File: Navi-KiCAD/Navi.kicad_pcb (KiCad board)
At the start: 4 copper layers, 50.8 x 40 mm, 207 parts, among them J1 0734120110, J2 0734120110, J3 0734120110, J4 473460001, J5 AXK5S80047YG, J6 AXK5S80047YG, Q1 IRLML5203PbF, Q2 IRLML5203PbF, U1 LP5521YQ/NOPB, U10 TPS54232DR, U11 MPU-9250, U12 LPS25HBTR, U13 NUF2042XV6T1G, U14 LTC4412ES6, U15 MIC94082YFT, U2 Logo, U3 Logo, U4 ATSAME70Q21A-AN, U5 CC1310F128RGZR, U6 CC1190RGVR, U7 CC2650F128RGZR, U8 CC2592RGVR, U9 MAX-M8W-0, Y1 9HT11-32.768KDZB-T, Y2 7V-16.000MAHJ-T, Y3 XRCGB24M000F2P00R0, Y4 XRCGB24M000F2P00R0

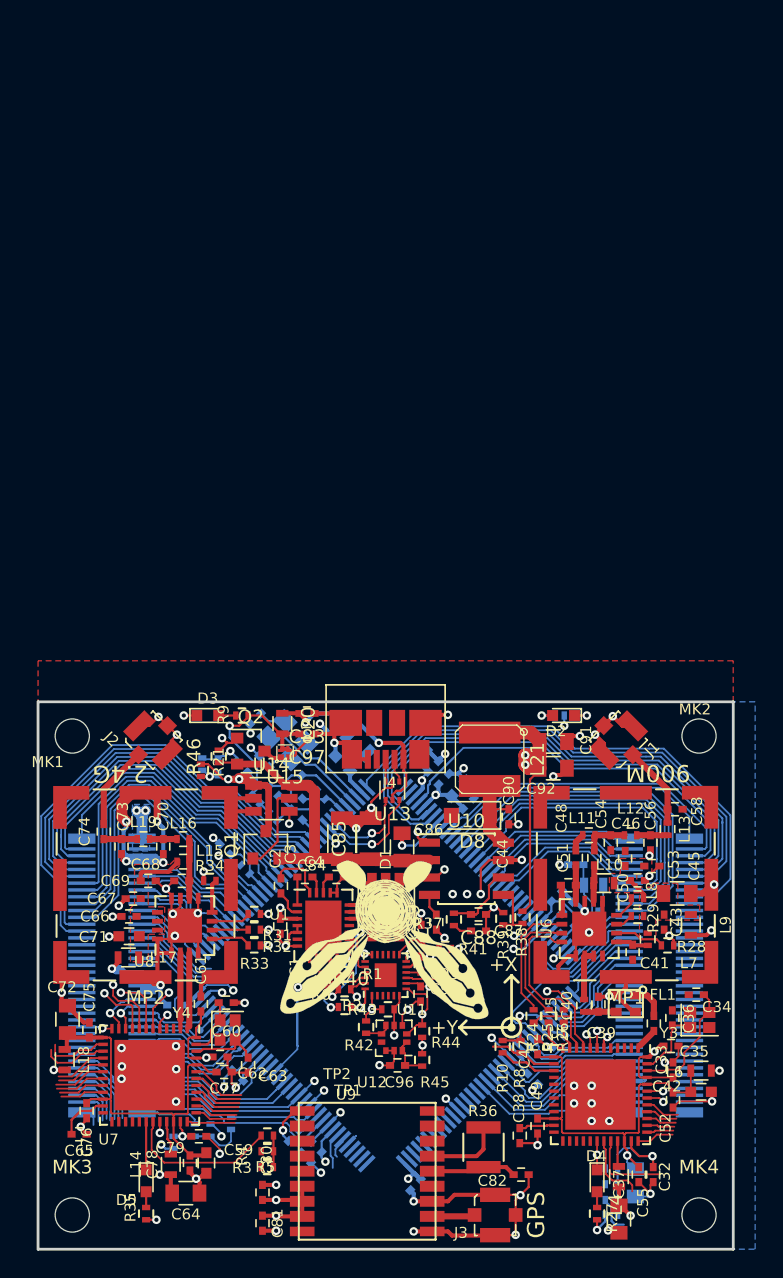
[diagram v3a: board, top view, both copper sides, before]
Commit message: Additional routing
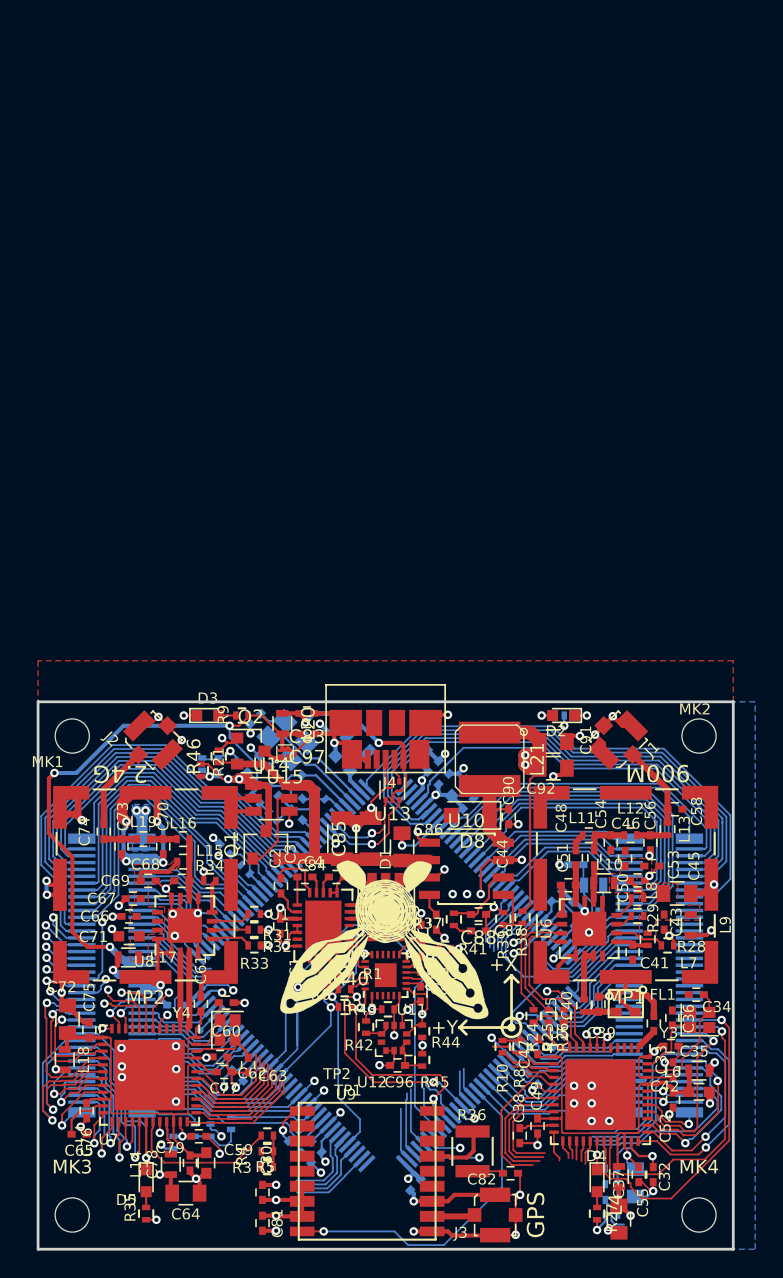
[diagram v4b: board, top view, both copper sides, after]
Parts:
- Q1, Q2: value IRLML5203PbF -> IRLML5203TRPBF
- U14: value LTC4412ES6 -> LTC4412ES6#TRPBF
- U15: value MIC94082YFT -> MIC94082YFT-TR
- moved R36 0.85 mm to (81.3, 117.8)
- moved C82 0.78 mm to (84.1, 119.5)
- moved C42 0.15 mm to (97.9, 113.5)
- moved L6 0.15 mm to (97.9, 112.0)
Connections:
- J5 pad 35: Net-(J5-Pad35) -> VUSB
- J5 pad 37: Net-(J5-Pad37) -> VUSB
- J5 pad 50: Net-(J5-Pad50) -> /Connectors/2.4-DIO-10
- J5 pad 52: Net-(J5-Pad52) -> /Connectors/2.4-DIO-9
- J5 pad 54: Net-(J5-Pad54) -> /Connectors/2.4-DIO-8
- J5 pad 58: Net-(J5-Pad58) -> /Connectors/2.4-DIO-20
- J5 pad 60: Net-(J5-Pad60) -> /Connectors/2.4-DIO-11
- J5 pad 62: Net-(J5-Pad62) -> /Connectors/2.4-DIO-19
- J5 pad 64: Net-(J5-Pad64) -> /Connectors/2.4-DIO-12
- J5 pad 66: Net-(J5-Pad66) -> /Connectors/2.4-DIO-18
- J5 pad 68: Net-(J5-Pad68) -> /Connectors/2.4-DIO-13
- J5 pad 70: Net-(J5-Pad70) -> /Connectors/2.4-DIO-17
- J5 pad 72: Net-(J5-Pad72) -> /Connectors/2.4-DIO-14
- J5 pad 74: Net-(J5-Pad74) -> /Connectors/2.4-DIO-16
- J5 pad 76: Net-(J5-Pad76) -> /2.4-TCKC
- J5 pad 78: Net-(J5-Pad78) -> /2.4-TMSC
- J5 pad 80: Net-(J5-Pad80) -> /Connectors/2.4-DIO-15
- J6 pad 28: Net-(J6-Pad28) -> /Connectors/PE5
- J6 pad 53: Net-(J6-Pad53) -> /Connectors/900-DIO-21
- J6 pad 55: Net-(J6-Pad55) -> /Connectors/900-DIO-22
- J6 pad 57: Net-(J6-Pad57) -> /Connectors/900-ADIO-27
- J6 pad 59: Net-(J6-Pad59) -> /Connectors/900-ADIO-23
- J6 pad 61: Net-(J6-Pad61) -> /Connectors/900-ADIO-24
- J6 pad 65: Net-(J6-Pad65) -> /Connectors/900-ADIO-26
- J6 pad 67: Net-(J6-Pad67) -> /Connectors/900-ADIO-25
- J6 pad 75: Net-(J6-Pad75) -> /Connectors/900-ADIO-30
- J6 pad 77: Net-(J6-Pad77) -> /Connectors/900-ADIO-29
- J6 pad 79: Net-(J6-Pad79) -> /Connectors/900-ADIO-28
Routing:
- net VUSB: track 15.0 -> 51.4 mm, vias 1 -> 3
- net /GNC_Processor/GPS-~RESET: track 0.00 -> 24.5 mm, vias 0 -> 1
- net /Connectors/900-DIO-21: track 5.19 -> 25.5 mm, vias 0 -> 1
- net /GNC_Processor/IMU-INT: track 0.68 -> 18.7 mm
- net /Connectors/900-DIO-22: track 6.02 -> 22.3 mm, vias 0 -> 1
- net /Connectors/PE5: track 0.00 -> 15.4 mm
- net /GNC_Processor/IMU-SPI-CLK: track 1.96 -> 17.0 mm, vias 1 -> 2
- net /GNC_Processor/IMU-SPI-MOSI: track 2.32 -> 17.1 mm, vias 1 -> 2
- net /Connectors/2.4-DIO-19: track 0.00 -> 13.4 mm, vias 0 -> 1
- net /Connectors/900-ADIO-23: track 2.72 -> 16.1 mm, vias 0 -> 1
- net /GNC_Processor/IMU-SPI-MISO: track 2.23 -> 15.2 mm, vias 0 -> 1
- net Net-(J6-Pad73): track 0.00 -> 12.7 mm
- net /Connectors/2.4-DIO-20: track 3.52 -> 16.0 mm, vias 0 -> 1
- net /Connectors/900-ADIO-24: track 1.97 -> 14.4 mm, vias 0 -> 1
- net /Connectors/2.4-DIO-11: track 3.70 -> 15.8 mm, vias 0 -> 1
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
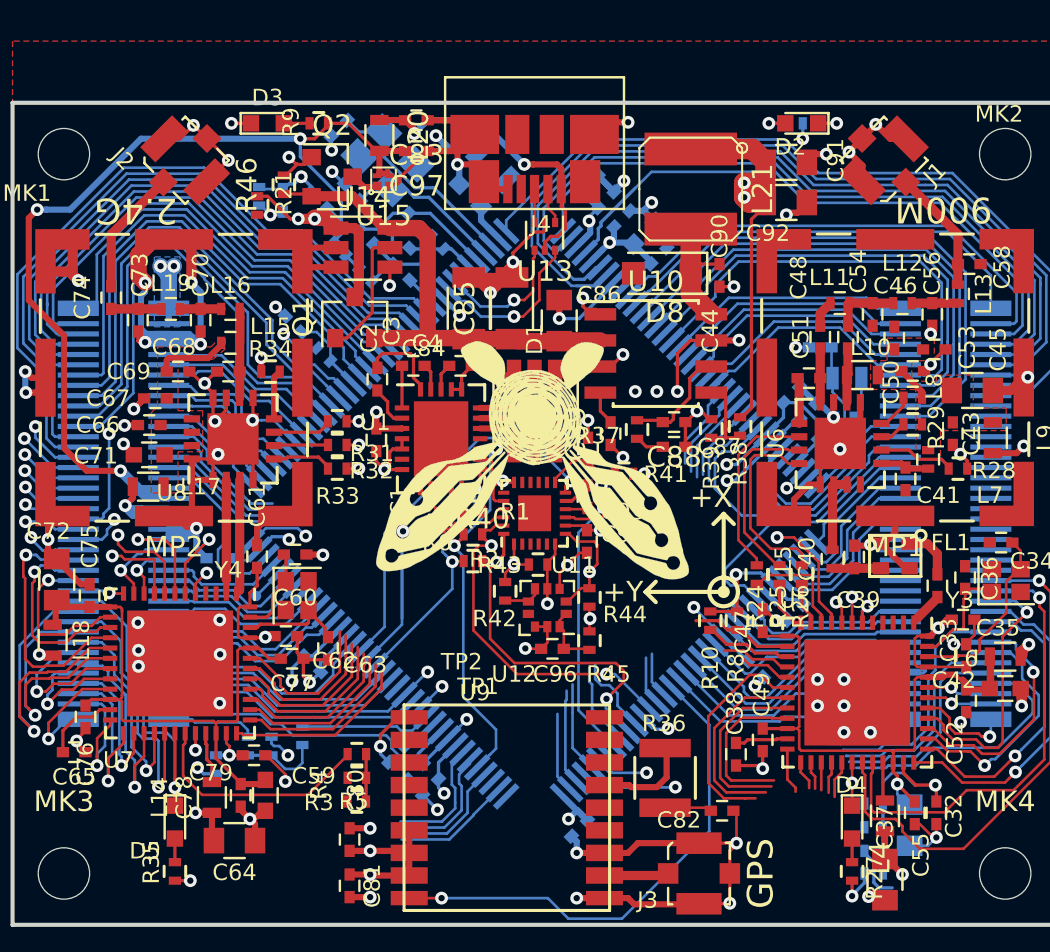
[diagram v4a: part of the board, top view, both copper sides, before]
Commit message: Upgraded to 9 channel RGB driver. Broke out signals for LSM303 and LSM6DS3
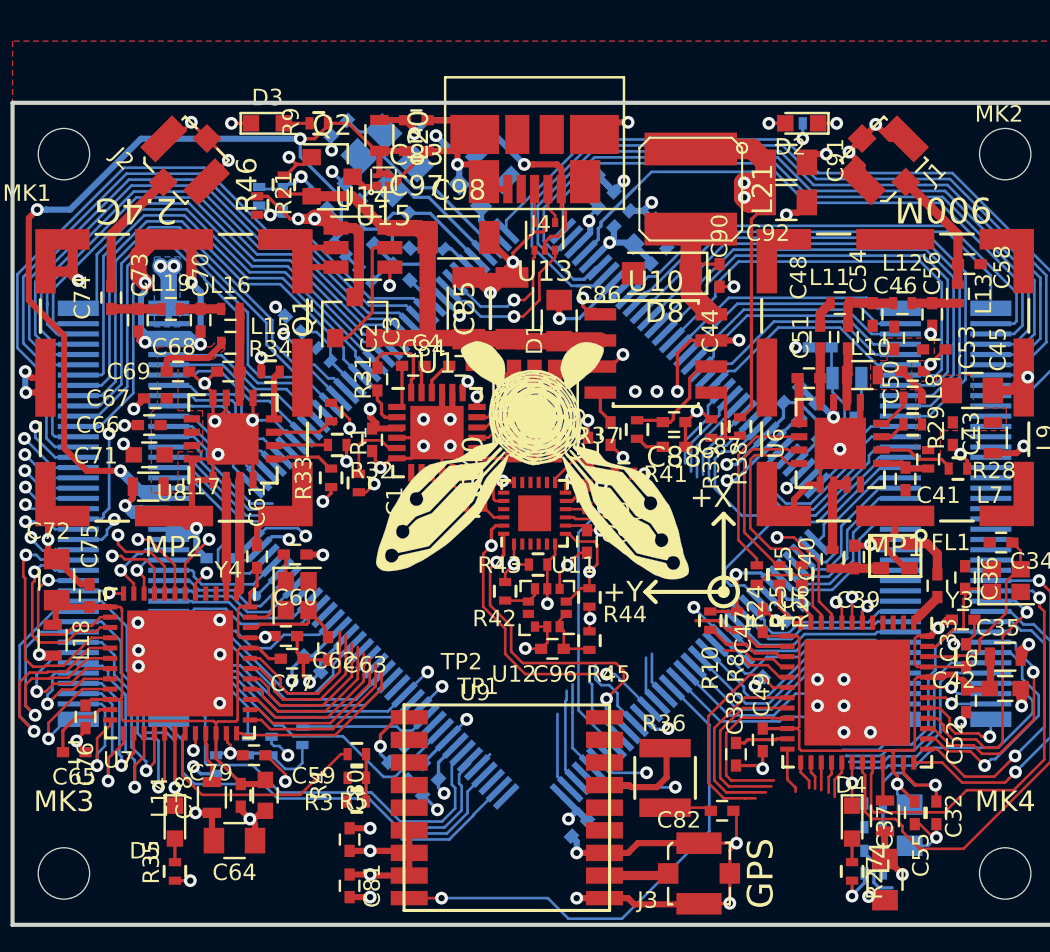
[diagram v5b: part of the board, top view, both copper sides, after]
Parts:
- removed R2, R6: 0 DNP, Resistors_SMD:R_0402
- added C98: GRM31CR61H106MA12L, Capacitors_SMD:C_1206, F.Cu at (71.3, 91.5)
- U1: value LP5521YQ/NOPB -> LP55231SQE/NOPB; footprint Housings_DFN_QFN:QFN-24-1EP_4x5mm_Pitch0.5mm -> Housings_DFN_QFN:QFN-24-1EP_4x4mm_Pitch0.5mm
- moved R1 5.72 mm to (66.5, 103.5), turned to 90 degrees
- moved R40 1.79 mm to (72.0, 104.6), turned to 0 degrees
- moved R31 0.54 mm to (65.1, 100.0), turned to 90 degrees
- moved R33 0.54 mm to (65.1, 103.2), turned to 270 degrees
- moved U1 0.36 mm to (70.2, 101.0)
- moved C1 0.20 mm to (67.1, 101.4)
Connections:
- net /Connectors/PB2 renamed /GNC_Processor/IMU-SPI-~CS2
- net /GNC_Processor/IMU-INT renamed /GNC_Processor/IMU-INT0
- net /GNC_Processor/IMU-SPI-~CS renamed /GNC_Processor/IMU-SPI-~CS0
- net Net-(U1-Pad16) renamed /LED_D4
- J5 pad 57: /Connectors/PD10 -> /Connectors/PC16
- J5 pad 59: /Connectors/PC16 -> /Connectors/PA1
- J5 pad 61: /Connectors/PA1 -> /Connectors/PC14
- J5 pad 63: /Connectors/PD11 -> /Connectors/PC11
- J5 pad 65: /Connectors/PC14 -> /Connectors/PC10
- J5 pad 67: /Connectors/PC11 -> /Connectors/PB7
- J5 pad 69: /Connectors/PC10 -> /Connectors/PB12
- J5 pad 71: /Connectors/PB7 -> /Connectors/PC9
- J5 pad 73: /Connectors/PB12 -> /Connectors/PC8
- J5 pad 75: /Connectors/PC9 -> /2.4_RESET_EXT
- J5 pad 77: /Connectors/PC8 -> /Connectors/PB6
- J5 pad 79: /2.4_RESET_EXT -> /Connectors/PD16
- U1 pad 10: (no net) -> GND
- U1 pad 11: (no net) -> /LED_D9R
- U1 pad 12: (no net) -> /LED_D8R
- U1 pad 13: /CPU-SDA -> Net-(D1-Pad4)
- U1 pad 14: Net-(R1-Pad2) -> Net-(D1-Pad5)
- U1 pad 15: /CPU-SCK -> Net-(D1-Pad6)
- U1 pad 17: Net-(D1-Pad4) -> /LED_D3
- U1 pad 18: Net-(D1-Pad5) -> /LED_D2
- U1 pad 19: Net-(D1-Pad6) -> /LED_D1
- U1 pad 25: (no net) -> GND
- U1 pad 5: GND -> Net-(R1-Pad2)
- U1 pad 6: Net-(U1-Pad6) -> GND
- U1 pad 7: GND -> Net-(U1-Pad7)
- U1 pad 8: (no net) -> /CPU-SDA
- U1 pad 9: (no net) -> /CPU-SCK
- U4 pad 101: /Connectors/PD10 -> /GNC_Processor/IMU-INT1
- U4 pad 47: /Connectors/PD27 -> /GNC_Processor/IMU-SPI-~CS1
- U4 pad 98: /Connectors/PD11 -> /GNC_Processor/IMU-INT2
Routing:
- net /CPU-SCK: track 27.5 -> 9.31 mm, vias 3 -> 1
- net /GNC_Processor/IMU-INT0: track 18.7 -> 0.88 mm
- net /Connectors/PB6: track 5.91 -> 20.9 mm
- net /Connectors/PD16: track 5.98 -> 20.7 mm
- net /GNC_Processor/IMU-SPI-~CS0: track 15.9 -> 1.27 mm, vias 1 -> 0
- net /CPU-SDA: track 20.6 -> 8.00 mm, vias 3 -> 1
- net /Connectors/PD11: track 8.86 -> 0.00 mm
- net /Connectors/PD10: track 7.37 -> 0.00 mm
- net GND: track 245.9 -> 251.1 mm, vias 91 -> 95
- net /LED_D4: track 0.00 -> 2.97 mm, vias 0 -> 1
- net /Connectors/PD26: track 14.4 -> 11.8 mm
- net /LED_D3: track 0.00 -> 2.06 mm, vias 0 -> 1
- net /LED_D9R: track 0.00 -> 1.86 mm, vias 0 -> 1
- net /GNC_Processor/IMU-SPI-CLK: track 17.0 -> 15.6 mm
- net /2.4_RESET_EXT: track 4.40 -> 5.73 mm
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
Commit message: Added additional sensors
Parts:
- added C100: 0.1u, Capacitors_SMD:C_0402, F.Cu at (89.0, 40.9)
- added C101: 0.1u, Capacitors_SMD:C_0402, F.Cu at (72.4, 59.0)
- added C102: 0.1u, Capacitors_SMD:C_0402, F.Cu at (74.1, 61.0)
- added C103: EMK105B7223KV-F, Capacitors_SMD:C_0402, F.Cu at (72.6, 62.6)
- added C104: EMK107BJ225KA-T, Capacitors_SMD:C_0603, F.Cu at (74.8, 59.0)
- added C99: 0.1u, Capacitors_SMD:C_0402, F.Cu at (87.2, 38.5)
- added R2: 10k, Resistors_SMD:R_0402, F.Cu at (85.0, 38.5)
- added R6: 47, Resistors_SMD:R_0402, F.Cu at (89.0, 38.9)
- added U16: LSM6DS33, Housings_LGA:LGA-16L_3x3mm_Pitch0.5mm, F.Cu at (86.5, 41.0)
- added U17: LSM303AH, Housings_LGA:LGA-12_2x2mm_Pitch0.5mm, F.Cu at (72.3, 60.8)

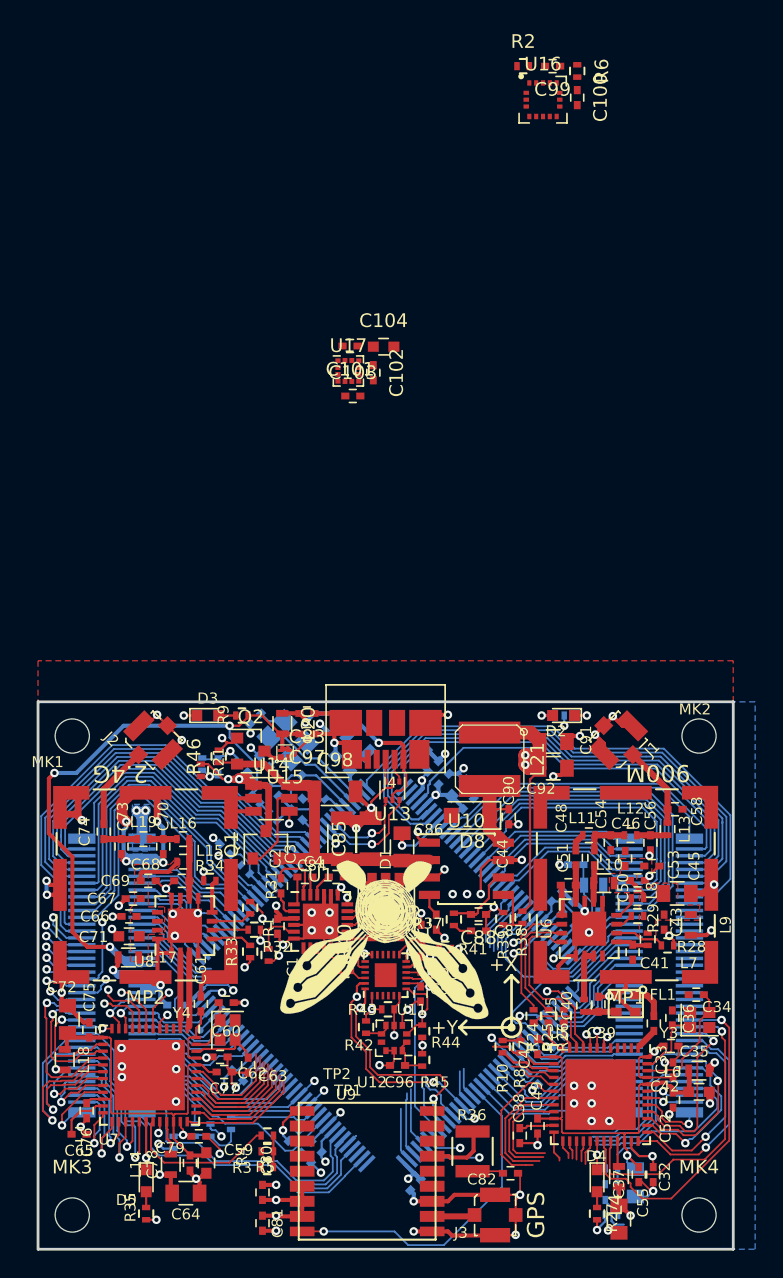
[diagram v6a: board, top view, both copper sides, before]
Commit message: Tweaked pinouts and finished routing known connectors. Now for the remaining IO.
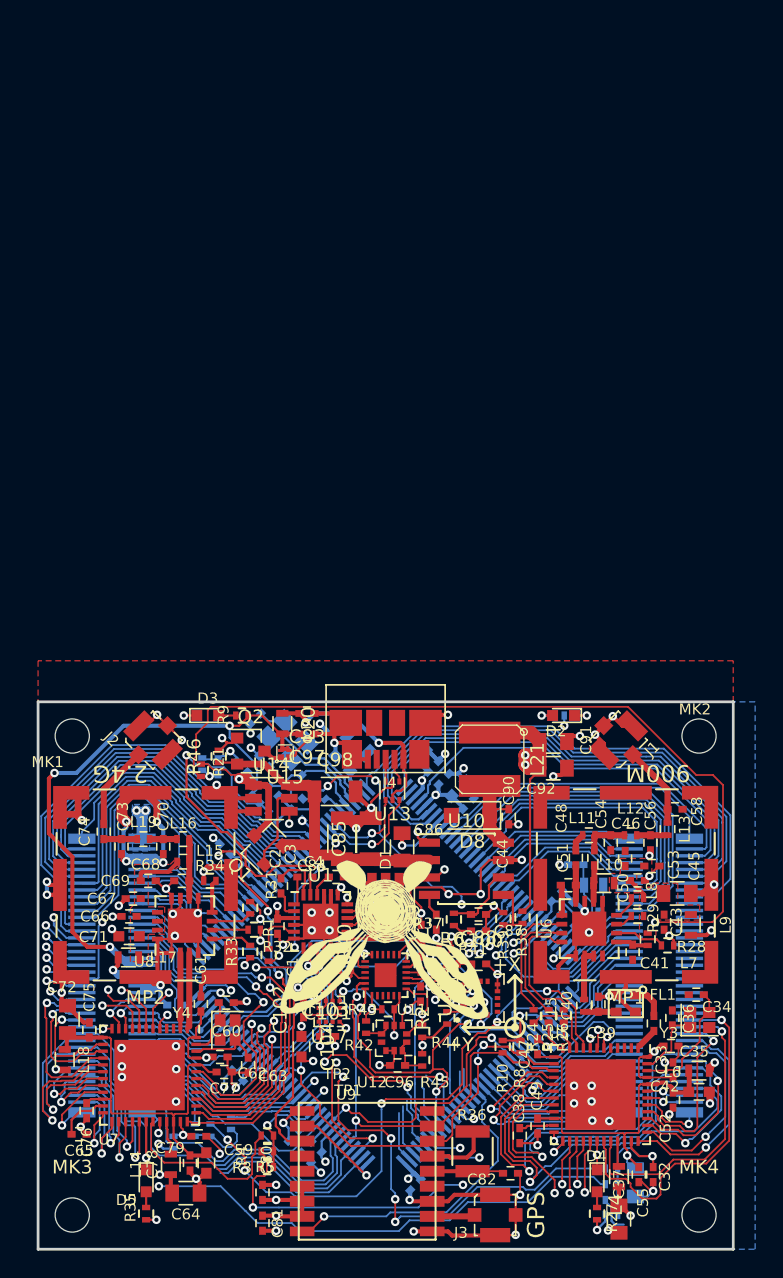
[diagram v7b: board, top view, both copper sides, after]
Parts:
- moved R2 69.8 mm to (79.5, 108.1), turned to 90 degrees
- moved C99 67.8 mm to (79.5, 105.9), turned to 270 degrees
- moved R6 65.9 mm to (79.8, 104.1), turned to 0 degrees
- moved U16 65.8 mm to (82.0, 106.6), turned to 90 degrees
- moved C100 63.7 mm to (81.8, 104.1), turned to 0 degrees
- moved C104 51.5 mm to (68.8, 110.2), turned to 270 degrees
- moved C101 50.5 mm to (70.8, 109.4), turned to 0 degrees
- moved C102 46.8 mm to (69.0, 107.5), turned to 90 degrees
- moved U17 46.8 mm to (70.9, 107.6), turned to 180 degrees
- moved C103 43.2 mm to (70.6, 105.8), turned to 180 degrees
- moved Q1 0.16 mm to (66.1, 95.5), turned to 135 degrees
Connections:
- net /GNC_Processor/IMU-SPI-~CS2 renamed /Connectors/PB2
- J5 pad 25: Net-(J5-Pad25) -> /Connectors/2.4-ADIO-24
- J5 pad 27: Net-(J5-Pad27) -> /Connectors/2.4-ADIO-23
- J5 pad 29: Net-(J5-Pad29) -> /Connectors/2.4-ADIO-25
- J5 pad 31: Net-(J5-Pad31) -> /Connectors/2.4-ADIO-30
- J6 pad 58: Net-(J6-Pad58) -> /Connectors/PA23
- J6 pad 60: /Connectors/PA23 -> /Connectors/PC7
- J6 pad 62: /Connectors/PD27 -> /Connectors/PA15
- J6 pad 63: Net-(J6-Pad63) -> /Connectors/900-DIO-15
- J6 pad 64: /Connectors/PC7 -> /Connectors/PA14
- J6 pad 66: /Connectors/PA15 -> /Connectors/PD25
- J6 pad 68: /Connectors/PA14 -> /Connectors/PD26
- J6 pad 69: Net-(J6-Pad69) -> /900-TMSC
- J6 pad 70: /Connectors/PD25 -> /Connectors/PC6
- J6 pad 71: Net-(J6-Pad71) -> /900-TCKC
- J6 pad 72: /Connectors/PD26 -> /Connectors/PD24
- J6 pad 73: Net-(J6-Pad73) -> /Connectors/900-DIO-13
- J6 pad 74: /Connectors/PC6 -> /Connectors/PA24
- J6 pad 76: /Connectors/PD24 -> /Connectors/900-DIO-10
- J6 pad 78: /Connectors/PA24 -> /Connectors/900-DIO-11
- J6 pad 80: Net-(J6-Pad80) -> /Connectors/900-DIO-12
- U17 pad 2: Net-(U17-Pad2) -> +3V3
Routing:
- net Net-(C12-Pad1): track 24.6 -> 108.5 mm, vias 6 -> 10
- net /GNC_Processor/VBATT: track 3.05 -> 72.1 mm, vias 2 -> 3
- net /CPU-SDA: track 8.00 -> 62.7 mm, vias 1 -> 5
- net /CPU-SCK: track 9.31 -> 59.3 mm, vias 1 -> 4
- net /900_RESET_2.4: track 0.88 -> 41.9 mm, vias 1 -> 2
- net /GNC_Processor/VBUS_DETECT: track 4.11 -> 42.8 mm, vias 1 -> 4
- net /2.4G-Rx: track 3.70 -> 42.2 mm, vias 1 -> 3
- net /CPU_RESET_900: track 0.91 -> 38.4 mm, vias 1 -> 3
- net /2.4_RESET_900: track 7.11 -> 44.0 mm, vias 2 -> 5
- net /900_RESET_CPU: track 0.00 -> 35.4 mm, vias 0 -> 4
- net /2.4G-Tx: track 4.49 -> 38.5 mm, vias 1 -> 3
- net /GNC_Processor/IMU-INT1: track 0.00 -> 28.0 mm, vias 0 -> 1
- net /2.4 GHz Radio/LNA_EN: track 2.04 -> 24.3 mm
- net GND: track 251.1 -> 271.9 mm, vias 95 -> 102
- net /Connectors/2.4-ADIO-24: track 8.23 -> 29.0 mm, vias 0 -> 1
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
